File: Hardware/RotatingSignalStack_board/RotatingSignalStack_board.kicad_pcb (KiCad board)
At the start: 2 copper layers, 102 x 46.2 mm, 34 parts, among them J1 8P8C_LED_Shielded, SW1 SW_Push, SW2 SW_Push, U1 OKI, U2 Teensy4.1_DEV-16771

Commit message: Made Rev2 + Gerbs + STEP
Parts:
- removed the G*** at (193.3, 82.0)
- removed the G*** at (128.3, 77.5)
- removed R3: 0, Resistor_SMD:R_0603_1608Metric_Pad0.98x0.95mm_HandSolder
- added G***: LOGO, MRDT_Silkscreens:0_MRDT_Logo_7.5mm, F.Cu at (186.9, 96.8)
- added G***: LOGO, MRDT_Silkscreens:0_MRDT_Logo_20mm, B.Cu at (164.8, 89.2)
- Conn3: value Molex_SL_05 -> Molex_SL_04; footprint MRDT_Connectors:MOLEX_SL_05_Horizontal -> MRDT_Connectors:MOLEX_SL_04_Horizontal
- G*** (x2): moved to F.Cu
- V1, V2, V3, V4: footprint MRDT_Drill_Holes:4_40_Hole_Corner -> MRDT_Drill_Holes:4_40_Hole
- moved V3 129.5 mm to (226.8, 119.4)
- moved V4 124.1 mm to (226.8, 81.3)
- moved V2 74.1 mm to (131.6, 119.4)
- moved V1 64.1 mm to (131.6, 81.3)
- moved J1 59.2 mm to (214.4, 75.1), turned to 180 degrees
- moved C6 56.7 mm to (224.5, 98.0), turned to -90 degrees
- moved R5 55.0 mm to (201.2, 97.5), turned to 90 degrees
- moved C2 54.8 mm to (158.0, 92.7), turned to 0 degrees
- moved R7 52.8 mm to (140.7, 120.7), turned to 0 degrees
- moved D4 51.7 mm to (144.8, 120.7), turned to 180 degrees
- moved C5 50.4 mm to (158.0, 80.0)
- moved U1 50.4 mm to (157.1, 88.9)
- moved R4 48.9 mm to (194.6, 97.5), turned to 90 degrees
- moved U2 48.7 mm to (191.5, 110.2)
- moved G*** 48.3 mm to (145.8, 108.7), turned to 0 degrees
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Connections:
- Conn3 pad 1: MAG ENABLE -> +3.3V
- Conn3 pad 2: I2C SDA -> GND
- Conn3 pad 4: GND -> I2C SDA
- Conn4 pad 1: HB_FWD -> HB_RVS
- Conn4 pad 2: HB_RVS -> HB_FWD
- R4 pad 1: COMP PWR -> I2C SCL
- R4 pad 2: I2C SDA -> +3.3V
- R5 pad 1: COMP PWR -> I2C SDA
- R5 pad 2: I2C SCL -> +3.3V
- U2 pad 0: JOG A -> unconnected-(U2-RX1-Pad0)
- U2 pad 1: JOG B -> unconnected-(U2-TX1-Pad1)
- U2 pad 18: MAG ENABLE -> unconnected-(U2-A4-Pad18)
- U2 pad 33: unconnected-(U2-MCLK2-Pad33) -> JOG A
- U2 pad 34: unconnected-(U2-RX8-Pad34) -> JOG B
- U2 pad 40: COMP PWR -> unconnected-(U2-A16-Pad40)
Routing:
- net +12V: track 46.1 -> 0.00 mm
- net JOG A: track 51.0 -> 14.4 mm
- net +3.3V: track 266.8 -> 291.9 mm, vias 1 -> 0
- net MAG ENABLE: track 21.5 -> 0.00 mm
- net COMP PWR: track 19.4 -> 0.00 mm
- net HB_RVS: track 15.1 -> 31.2 mm
- net HB_FWD: track 15.1 -> 31.2 mm
- net /LED: track 32.3 -> 47.0 mm
- net /Tx+: track 22.5 -> 34.7 mm
- net /Tx-: track 23.0 -> 34.6 mm
- net JOG B: track 37.7 -> 29.3 mm
- net /Rx+: track 15.6 -> 24.0 mm
- net /Rx-: track 15.8 -> 24.0 mm
- net I2C SCL: track 23.2 -> 30.7 mm
- net I2C SDA: track 26.7 -> 30.7 mm, vias 2 -> 0
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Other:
- board size 102 x 46.2 mm -> 103.4 x 46.2 mm
- board text added: "Signal Stack Board, Rev2 Mars Rover Design Team Missouri S&T, 2024 Grant Brinker"
- board text removed: "12V"
- board text removed: "Compass"
- board text removed: "ENB"
- board text removed: "H-Bridge"
- board text removed: "Signal Stack Board, Rev1 Mars Rover Design Team Missouri S&T, 2024 Grant Brinker"

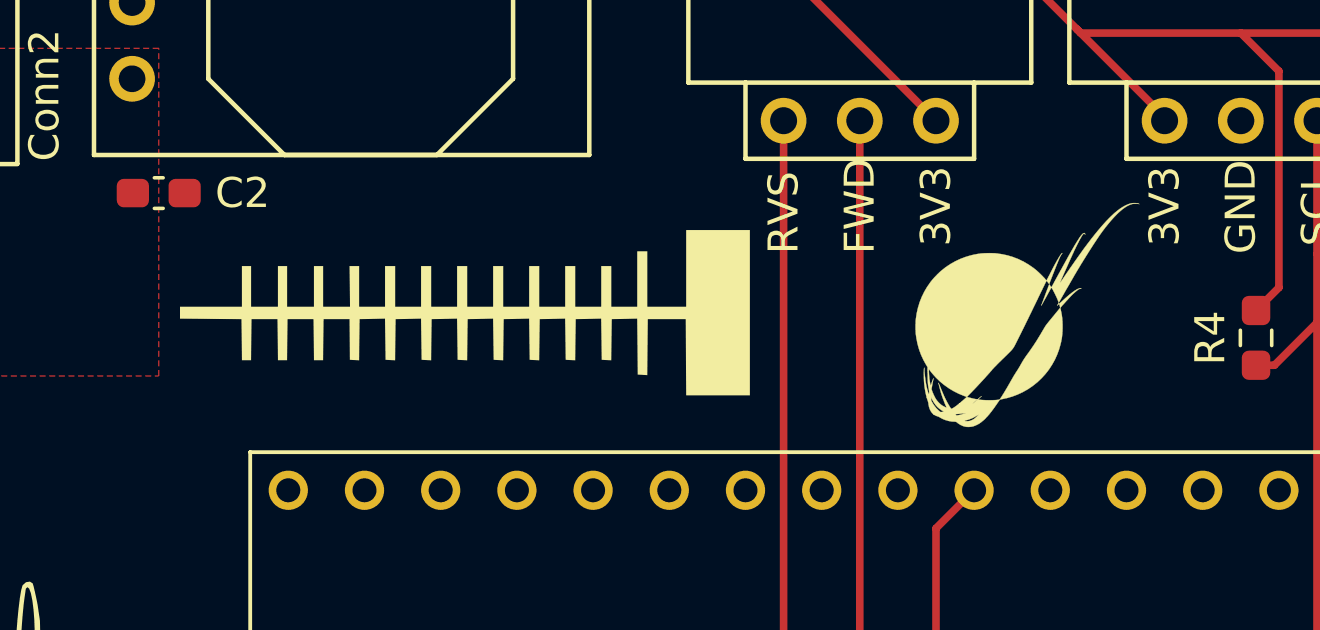
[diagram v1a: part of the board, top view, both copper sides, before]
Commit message: Updated silkscreen
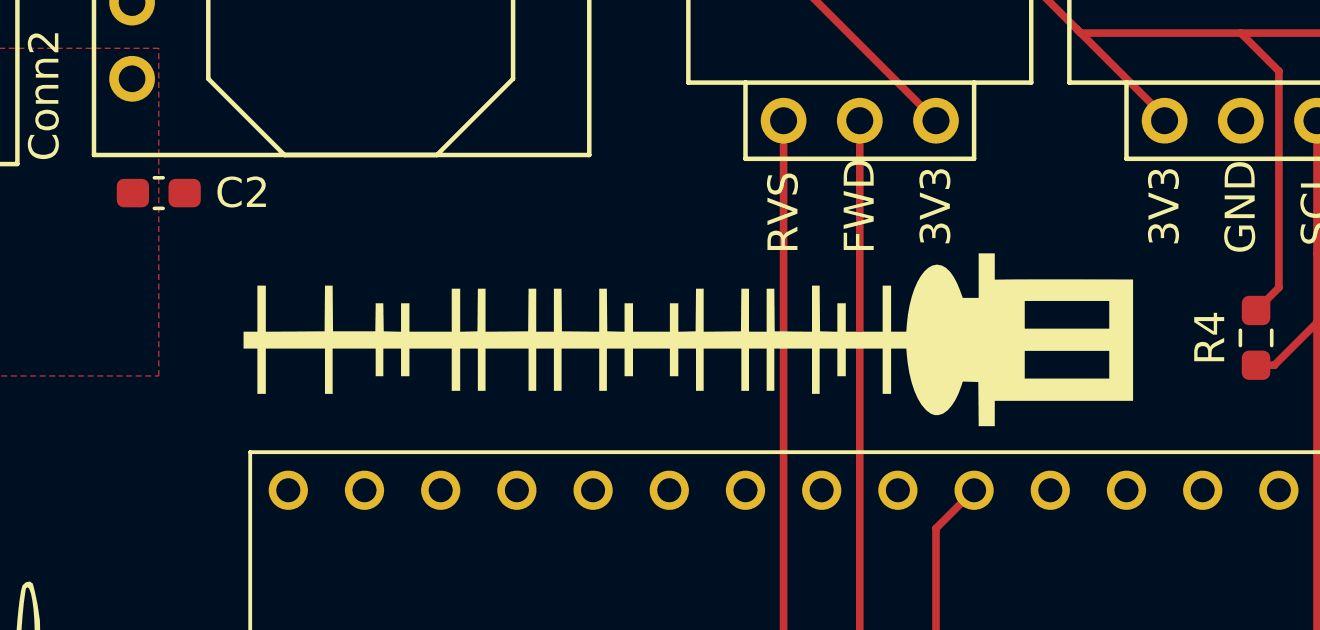
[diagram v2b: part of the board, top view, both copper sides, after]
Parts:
- removed the G*** at (186.9, 96.8)
- removed the G*** at (168.1, 96.8)
- added G***: LOGO, MRDT_Silkscreens:yagi2_30mm, F.Cu at (175.8, 97.7)

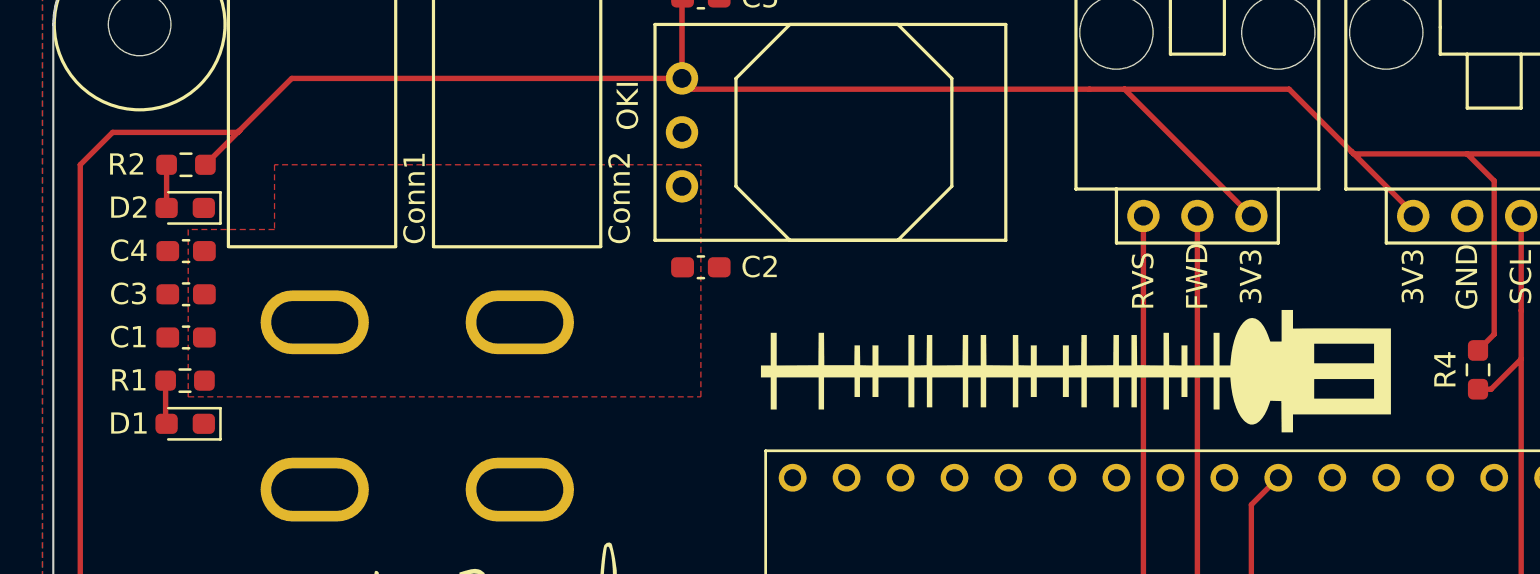
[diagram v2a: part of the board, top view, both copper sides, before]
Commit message: Changed 22uF cap + remade Gerbs and STEP
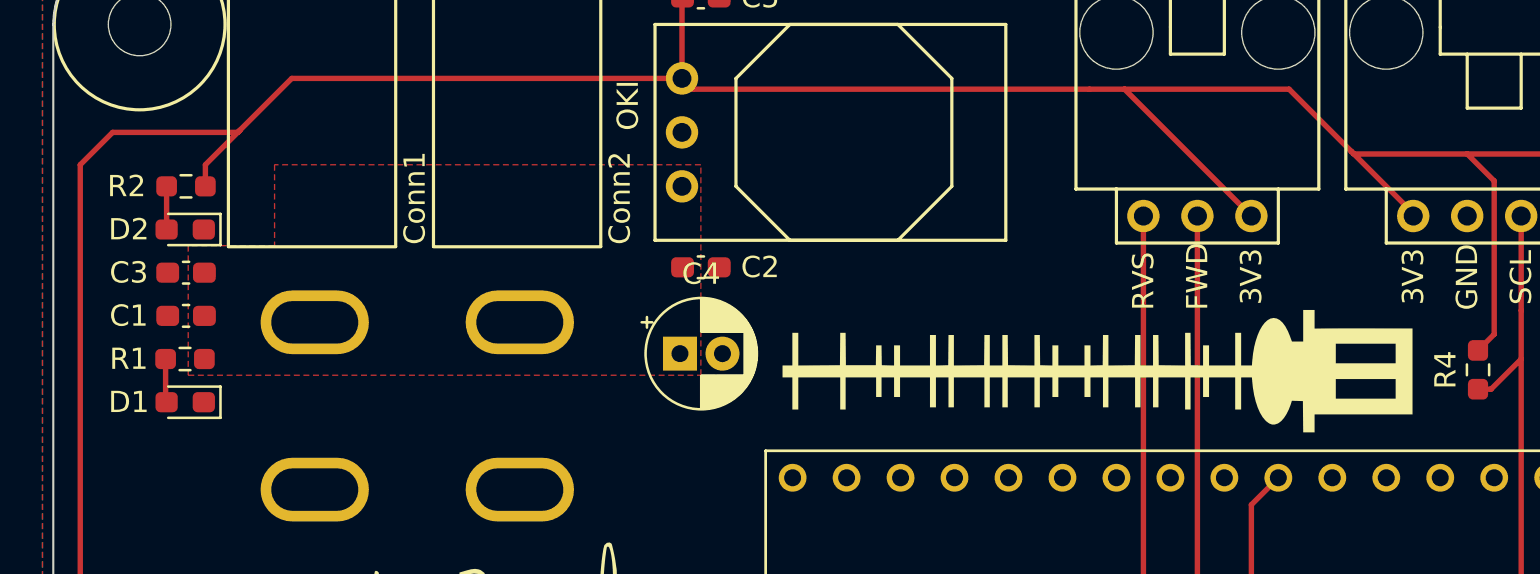
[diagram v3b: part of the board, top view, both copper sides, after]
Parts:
- C4: footprint Capacitor_SMD:C_0603_1608Metric_Pad1.08x0.95mm_HandSolder -> Capacitor_THT:CP_Radial_D5.0mm_P2.00mm
- moved C4 23.7 mm to (157.0, 96.8), turned to 0 degrees
- moved C1 1.02 mm to (133.8, 95.0)
- moved C3 1.02 mm to (133.8, 93.0)
- moved D2 1.02 mm to (133.7, 90.9)
- moved R2 1.02 mm to (133.8, 88.9)
- moved D1 1.02 mm to (133.7, 99.1)
- moved G*** 1.02 mm to (176.8, 97.7)
- moved R1 1.02 mm to (133.7, 97.0)
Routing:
- net +3.3V: track 291.9 -> 292.9 mm
